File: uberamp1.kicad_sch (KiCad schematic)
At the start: 0 parts

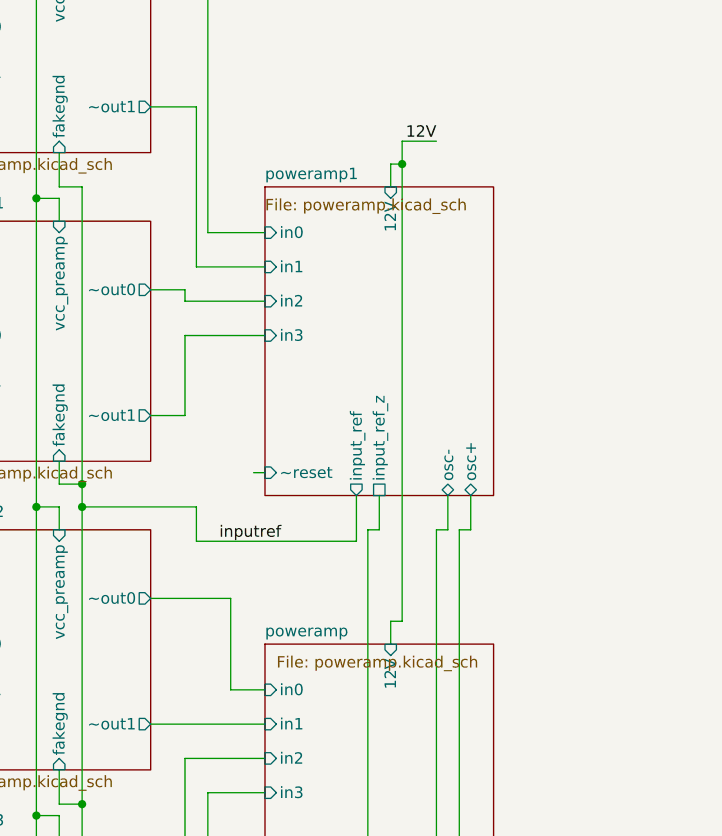
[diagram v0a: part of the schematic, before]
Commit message: add bypass caps to opamps + swap poweramps + layout progress
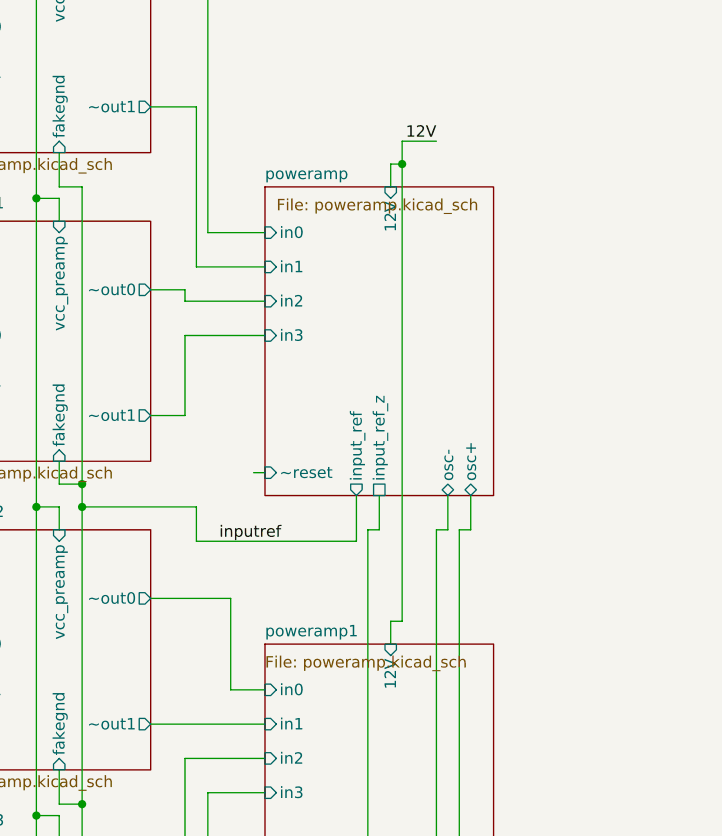
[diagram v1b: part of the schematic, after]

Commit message: route 1 preamp
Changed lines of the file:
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@@
     (effects (font (size 1.27 1.27)) (justify left bottom))
+  )
+  (label "~fb1" (at 180.34 57.15 0) (fields_autoplaced)
+    (effects (font (size 1.016 1.016)) (justify left bottom))
   )
   (label "12V" (at 167.64 13.97 180) (fields_autoplaced)
     (effects (font (size 1.27 1.27)) (justify right bottom))
   )
+  (label "fb0" (at 179.07 22.86 0) (fields_autoplaced)
+    (effects (font (size 1.016 1.016)) (justify left bottom))
+  )
+  (label "~fb0" (at 179.07 25.4 0) (fields_autoplaced)
+    (effects (font (size 1.016 1.016)) (justify left bottom))
+  )
+  (label "fb1" (at 180.34 54.61 0) (fields_autoplaced)
+    (effects (font (size 1.016 1.016)) (justify left bottom))
+  )
   (label "inputref" (at 161.29 78.74 0) (fields_autoplaced)

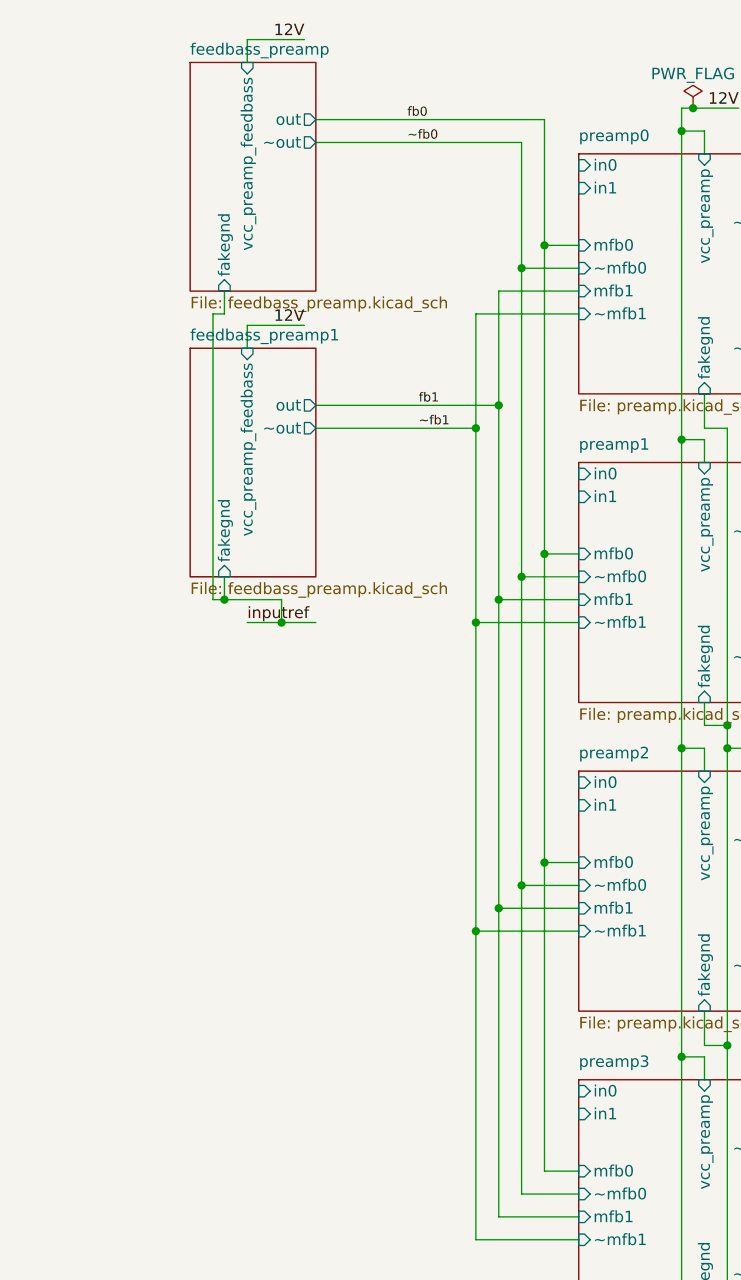
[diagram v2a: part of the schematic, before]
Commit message: add dacs to schematic
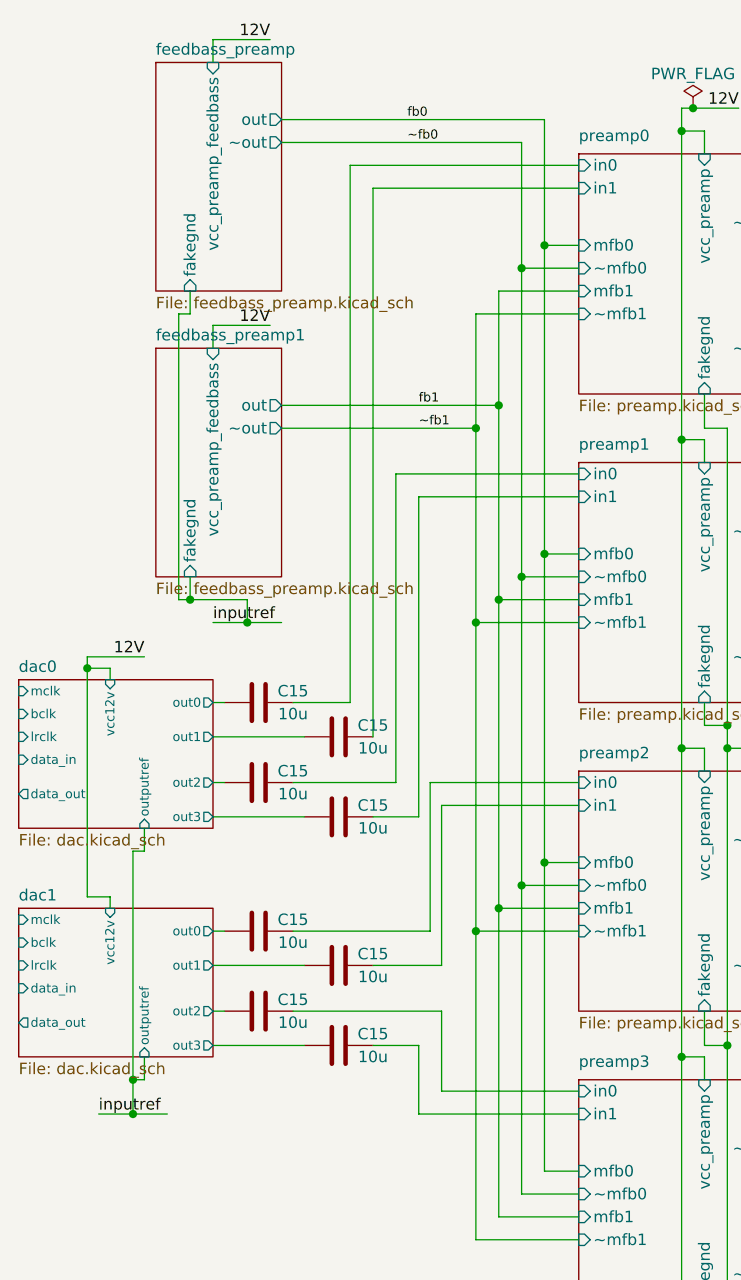
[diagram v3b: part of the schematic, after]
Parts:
- added C15 (x8): 10u, invendelirium_audio:C_0603, symbol Device:C
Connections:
- net preamp0/in0: now also C15.2
- net preamp0/in1: now also C15.2
- net preamp1/in0: now also C15.2
- net preamp1/in1: now also C15.2
- net preamp2/in0: now also C15.2
- net preamp2/in1: now also C15.2
- net preamp3/in0: now also C15.2
- net preamp3/in1: now also C15.2
- new net dac0/out0: C15.1
- new net dac0/out1: C15.1
- new net dac0/out2: C15.1
- new net dac0/out3: C15.1
- new net dac1/out0: C15.1
- new net dac1/out1: C15.1
- new net dac1/out2: C15.1
- new net dac1/out3: C15.1
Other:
- added sheet dac0 (dac.kicad_sch)
- added sheet dac1 (dac.kicad_sch)

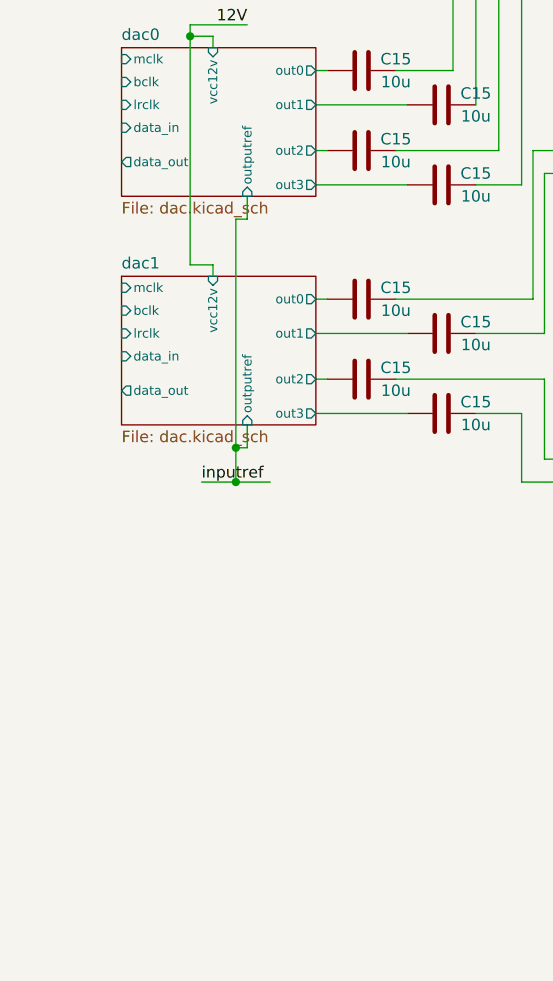
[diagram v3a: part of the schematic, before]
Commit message: add step-down regulators to schematic
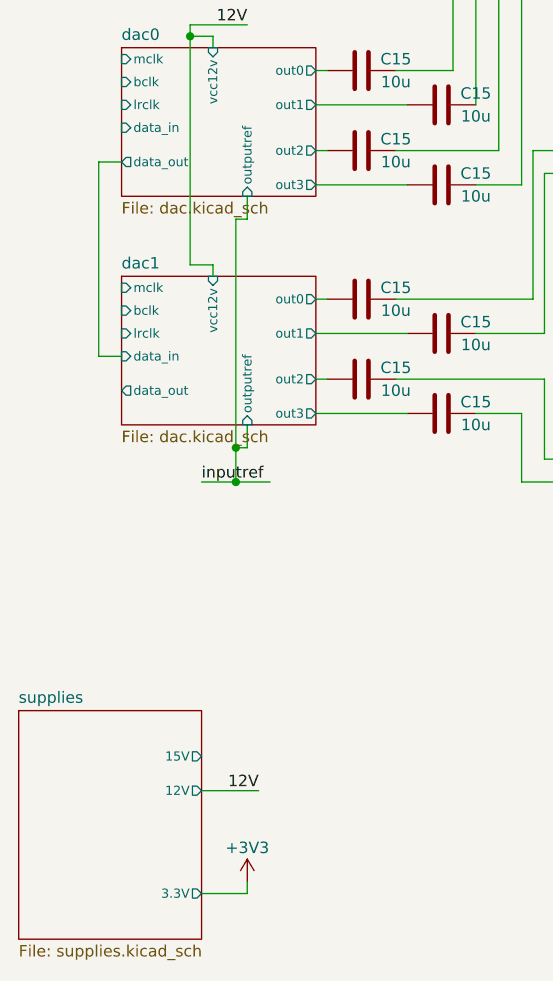
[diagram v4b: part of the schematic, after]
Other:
- added sheet supplies (supplies.kicad_sch)
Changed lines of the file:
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@@
+    (stroke (width 0) (type default))
+  )
+  (wire (pts (xy 135.89 97.79) (xy 133.35 97.79))
     (stroke (width 0) (type default))
   )
@@
     (stroke (width 0) (type default))
   )
+  (wire (pts (xy 133.35 97.79) (xy 133.35 119.38))
+    (stroke (width 0) (type default))
+  )
   (wire (pts (xy 247.65 91.44) (xy 247.65 95.25))
     (stroke (width 0) (type default))
@@
     (stroke (width 0) (type default))
   )
+  (wire (pts (xy 149.86 179.07) (xy 149.86 177.8))
+    (stroke (width 0) (type default))
+  )
   (wire (pts (xy 209.55 58.42) (xy 209.55 92.71))
     (stroke (width 0) (type default))
@@
     (stroke (width 0) (type default))
   )
+  (wire (pts (xy 144.78 179.07) (xy 149.86 179.07))
+    (stroke (width 0) (type default))
+  )
   (wire (pts (xy 146.05 83.82) (xy 146.05 85.09))
     (stroke (width 0) (type default))
   )
+  (wire (pts (xy 144.78 167.64) (xy 151.13 167.64))
+    (stroke (width 0) (type default))
+  )
   (wire (pts (xy 189.23 110.49) (xy 189.23 76.2))
     (stroke (width 0) (type default))
@@
   )
   (wire (pts (xy 212.09 57.15) (xy 214.63 57.15))
+    (stroke (width 0) (type default))
+  )
+  (wire (pts (xy 133.35 119.38) (xy 135.89 119.38))
     (stroke (width 0) (type default))
   )
@@
   (label "~fb1" (at 180.34 57.15 0) (fields_autoplaced)
     (effects (font (size 1.016 1.016)) (justify left bottom))
+  )
+  (label "12V" (at 151.13 167.64 180) (fields_autoplaced)
+    (effects (font (size 1.27 1.27)) (justify right bottom))
   )
   (label "12V" (at 163.83 13.97 180) (fields_autoplaced)
@@
         (path "/310059c1-d84b-43e2-9c9a-0e426c534a12"
           (reference "#FLG02") (unit 1)
+        )
+      )
+    )
+  )
+  (symbol (lib_id "power:+3V3") (at 149.86 177.8 0) (unit 1)
+    (in_bom yes) (on_board yes) (dnp no) (fields_autoplaced)
+    (property "Reference" "#PWR092" (at 149.86 181.61 0)
+      (effects (font (size 1.27 1.27)) hide)
+    )
+    (property "Value" "+3V3" (at 149.86 173.99 0)
+      (effects (font (size 1.27 1.27)))
+    )
+    (property "Footprint" "" (at 149.86 177.8 0)
+      (effects (font (size 1.27 1.27)) hide)
+    )
+    (property "Datasheet" "" (at 149.86 177.8 0)
+      (effects (font (size 1.27 1.27)) hide)
+    )
+    (pin "1")
+    (instances
+      (project "uberamp1"
+        (path "/310059c1-d84b-43e2-9c9a-0e426c534a12/9338c448-a5fc-4246-a946-e7fc08f9b36f"
+          (reference "#PWR092") (unit 1)
+        )
+        (path "/310059c1-d84b-43e2-9c9a-0e426c534a12/7069641c-0ed4-4995-a63e-1f44999c4edd"
+          (reference "#PWR0115") (unit 1)
+        )
+        (path "/310059c1-d84b-43e2-9c9a-0e426c534a12"
+          (reference "#PWR0143") (unit 1)
         )
       )
@@
       )
     )
+  )
+  (sheet (at 124.46 158.75) (size 20.32 25.4) (fields_autoplaced)
+    (stroke (width 0.1524) (type solid))
+    (fill (color 0 0 0 0.0000))
+    (property "Sheetname" "supplies" (at 124.46 158.0384 0)
+      (effects (font (size 1.27 1.27)) (justify left bottom))
+    )
+    (property "Sheetfile" "supplies.kicad_sch" (at 124.46 184.7346 0)
+      (effects (font (size 1.27 1.27)) (justify left top))
+    )
+    (pin "15V" output (at 144.78 163.83 0)
+      (effects (font (size 1.016 1.016)) (justify right))
+    )
+    (pin "3.3V" output (at 144.78 179.07 0)
+      (effects (font (size 1.016 1.016)) (justify right))
+    )
+    (pin "12V" output (at 144.78 167.64 0)
+      (effects (font (size 1.016 1.016)) (justify right))
+    )
+    (instances
+      (project "uberamp1"
+        (path "/310059c1-d84b-43e2-9c9a-0e426c534a12" (page "16"))
+      )
+    )
